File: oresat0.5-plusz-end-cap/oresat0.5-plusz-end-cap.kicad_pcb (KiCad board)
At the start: 2 copper layers, 105.6 x 105.6 mm, 43 parts, among them J2 U.FL-R-SMA, U1 LTC4305, U2 MMC5983MA, U3 MMC5983MA

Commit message: Oresat 0.5 +z end cap v1.3 ready for ordering!
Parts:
- removed @HOLE0, @HOLE1, @HOLE2, @HOLE3, @HOLE6, @HOLE7: MountingHole_2.1mm, MountingHole:MountingHole_2.1mm
- added @HOLE4: MountingHole_2.1mm, MountingHole:MountingHole_2.1mm, F.Cu at (198.0, 132.5)
- added @HOLE4: MountingHole_2.1mm, MountingHole:MountingHole_2.1mm, F.Cu at (176.0, 55.5)
- added @HOLE4: MountingHole_2.1mm, MountingHole:MountingHole_2.1mm, F.Cu at (198.0, 77.5)
- added @HOLE4: MountingHole_2.1mm, MountingHole:MountingHole_2.1mm, F.Cu at (121.0, 154.5)
- added @HOLE4: MountingHole_2.1mm, MountingHole:MountingHole_2.1mm, F.Cu at (176.0, 154.5)
- added @HOLE4: MountingHole_2.1mm, MountingHole:MountingHole_2.1mm, F.Cu at (121.0, 55.5)
- added LOGO1: , oresat-graphics:PSAS_LOGO_10X10, F.Cu at (183.5, 148.2)
- added REF**: logo-small, oresat-graphics:logo-small, F.Cu at (192.8, 139.0)
- C1, C10, C2, C3, C7: value ~ -> 100n
- C12, C13, C4: value ~ -> 10u
- D2, J1, R1, R10, R3, R4, R5, R6, R7, R8, R9: value ~ -> 4.7k
- R2: value ~ -> 2.7k
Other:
- board text added: "2024/03/20"
- board text removed: "2024/03/04"

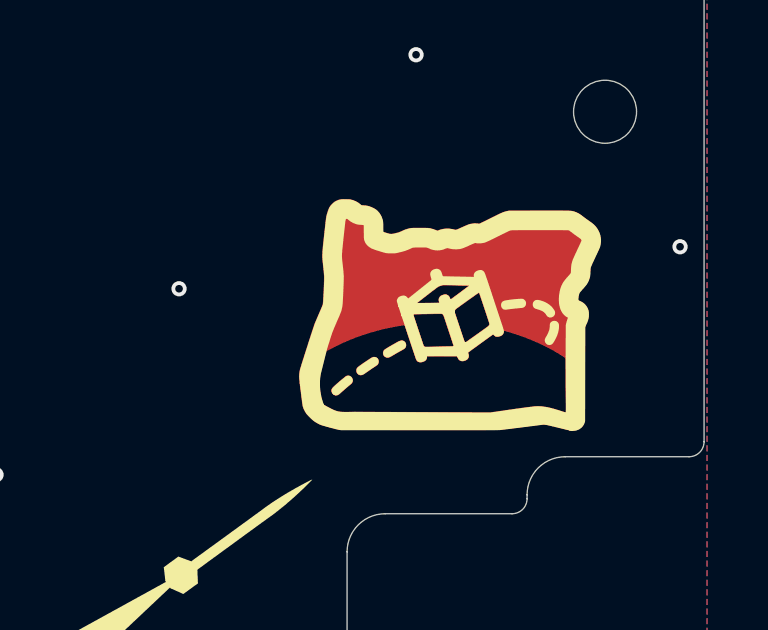
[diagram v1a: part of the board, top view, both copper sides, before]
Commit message: OreSat 0.5 Endcaps (+Z v1.3 and -Z v1.2) ready for ordering, reviewed -Z endcap, made small library and neatness changes to +Z endcap
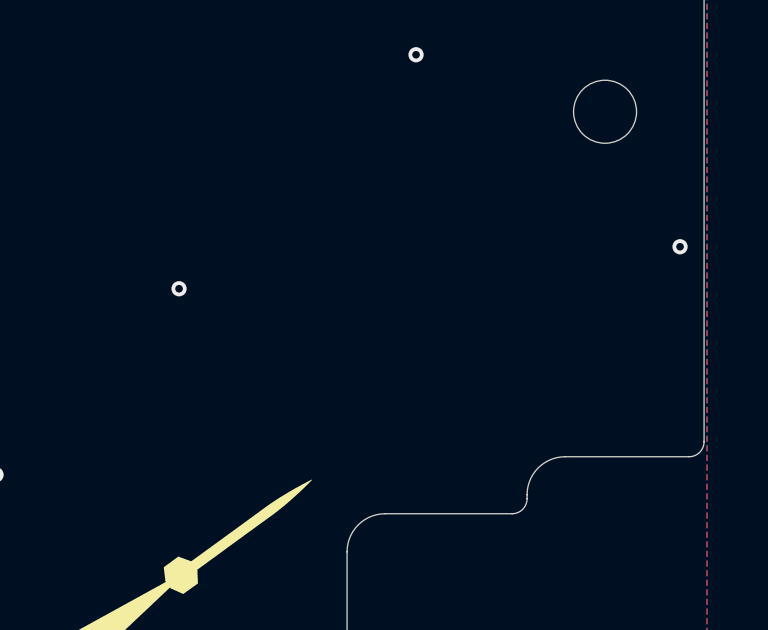
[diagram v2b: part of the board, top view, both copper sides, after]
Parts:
- removed REF**: logo-small, oresat-graphics:logo-small
- U1: footprint oresat0.5-plusz-end-cap:16-SSOP -> oresat-ics:16-SSOP

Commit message: Fixed issues 5 and 6 -- weird 4.7k values everywhere, missing libraries, and used no-place to indicate actual no place components.
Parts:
- D2: value 4.7k -> GRN
- J1: value 4.7k -> M55-7011242R
- R11, R12: value NP -> 2.7k
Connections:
- net 3.3V renamed +3.3V
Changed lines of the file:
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@@
 	)
 	(net 0 "")
-	(net 1 "3.3V")
+	(net 1 "+3.3V")
 	(net 2 "GND")
 	(net 3 "Net-(ANT1-A)")
@@
 		(sheetname "Root")
 		(sheetfile "oresat0.5-plusz-end-cap.kicad_sch")
-		(attr smd)
+		(attr smd dnp)
 		(fp_line
 			(start -0.885 -1.4)
@@
 			(layers "*.Cu" "*.Mask")
 			(remove_unused_layers no)
-			(net 1 "3.3V")
+			(net 1 "+3.3V")
 			(pinfunction "1")
 			(pintype "passive")
@@
 		(sheetname "Root")
 		(sheetfile "oresat0.5-plusz-end-cap.kicad_sch")
-		(attr smd)
+		(attr smd dnp)
 		(fp_rect
 			(start -1.4 3.1)
@@
 			)
 		)
-		(property "Value" "4.7k"
+		(property "Value" "GRN"
 			(at 0 0.635 0)
 			(layer "F.Fab")
@@
 			)
 		)
-		(property "Value" "4.7k"
+		(property "Value" "M55-7011242R"
 			(at 0 0 90)
 			(layer "B.Fab")
@@
 			(size 0.8 1.1)
 			(layers "B.Cu" "B.Paste" "B.Mask")
-			(net 1 "3.3V")
+			(net 1 "+3.3V")
 			(pinfunction "5")
 			(pintype "passive")
@@
 			(size 0.8 1.1)
 			(layers "B.Cu" "B.Paste" "B.Mask")
-			(net 1 "3.3V")
+			(net 1 "+3.3V")
 			(pinfunction "6")
 			(pintype "passive")
@@
 			(layers "B.Cu" "B.Paste" "B.Mask")
 			(roundrect_rratio 0.25)
-			(net 1 "3.3V")
+			(net 1 "+3.3V")
 			(pinfunction "2")
 			(pintype "passive")
@@
 			(layers "B.Cu" "B.Paste" "B.Mask")
 			(roundrect_rratio 0.25)
-			(net 1 "3.3V")
+			(net 1 "+3.3V")
 			(pinfunction "1")
 			(pintype "passive")
@@
 			(layers "B.Cu" "B.Paste" "B.Mask")
 			(roundrect_rratio 0.25)
-			(net 1 "3.3V")
+			(net 1 "+3.3V")
 			(pinfunction "1")
 			(pintype "passive")
@@
 			(layers "B.Cu" "B.Paste" "B.Mask")
 			(roundrect_rratio 0.25)
-			(net 1 "3.3V")
+			(net 1 "+3.3V")
 			(pinfunction "2")
 			(pintype "passive")
@@
 			(layers "B.Cu" "B.Paste" "B.Mask")
 			(roundrect_rratio 0.25)
-			(net 1 "3.3V")
+			(net 1 "+3.3V")
 			(pinfunction "2")
 			(pintype "passive")
@@
 			)
 		)
-		(property "Value" "NP"
+		(property "Value" "2.7k"
 			(at -1.2 -1.6 90)
 			(layer "B.Fab")
@@
 		(sheetname "Root")
 		(sheetfile "oresat0.5-plusz-end-cap.kicad_sch")
+		(attr dnp)
 		(fp_line
 			(start 1.495 -0.745)
@@
 			(layers "B.Cu" "B.Paste" "B.Mask")
 			(roundrect_rratio 0.25)
-			(net 1 "3.3V")
+			(net 1 "+3.3V")
 			(pinfunction "2")
 			(pintype "passive")
@@
 			(size 0.3 0.45)
 			(layers "B.Cu" "B.Paste" "B.Mask")
-			(net 1 "3.3V")
+			(net 1 "+3.3V")
 			(pinfunction "VDD")
 			(pintype "power_in")
@@
 			(size 0.3 0.45)
 			(layers "B.Cu" "B.Paste" "B.Mask")
-			(net 1 "3.3V")
+			(net 1 "+3.3V")
 			(pinfunction "SPI_CS")
 			(pintype "input")
@@
 			(size 0.3 0.45)
 			(layers "B.Cu" "B.Paste" "B.Mask")
-			(net 1 "3.3V")
+			(net 1 "+3.3V")
 			(pinfunction "VDDIO")
 			(pintype "power_in")
@@
 			(size 0.3 0.45)
 			(layers "B.Cu" "B.Paste" "B.Mask")
-			(net 1 "3.3V")
+			(net 1 "+3.3V")
 			(pinfunction "VDD")
 			(pintype "power_in")
@@
 			(size 0.3 0.45)
 			(layers "B.Cu" "B.Paste" "B.Mask")
-			(net 1 "3.3V")
+			(net 1 "+3.3V")
 			(pinfunction "SPI_CS")
 			(pintype "input")
@@
 			(size 0.3 0.45)
 			(layers "B.Cu" "B.Paste" "B.Mask")
-			(net 1 "3.3V")
+			(net 1 "+3.3V")
 			(pinfunction "VDDIO")
 			(pintype "power_in")
@@
 			(layers "B.Cu" "B.Paste" "B.Mask")
 			(roundrect_rratio 0.25)
-			(net 1 "3.3V")
+			(net 1 "+3.3V")
 			(pinfunction "2")
 			(pintype "passive")
@@
 			(layers "B.Cu" "B.Paste" "B.Mask")
 			(roundrect_rratio 0.25)
-			(net 1 "3.3V")
+			(net 1 "+3.3V")
 			(pinfunction "1")
 			(pintype "passive")
@@
 			(layers "B.Cu" "B.Paste" "B.Mask")
 			(roundrect_rratio 0.25)
-			(net 1 "3.3V")
+			(net 1 "+3.3V")
 			(pinfunction "2")
 			(pintype "passive")
@@
 			(layers "B.Cu" "B.Paste" "B.Mask")
 			(roundrect_rratio 0.25)
-			(net 1 "3.3V")
+			(net 1 "+3.3V")
 			(pinfunction "1")
 			(pintype "passive")
@@
 			(layers "B.Cu" "B.Paste" "B.Mask")
 			(roundrect_rratio 0.25)
-			(net 1 "3.3V")
+			(net 1 "+3.3V")
 			(pinfunction "1")
 			(pintype "passive")
@@
 			(layers "B.Cu" "B.Paste" "B.Mask")
 			(roundrect_rratio 0.25)
-			(net 1 "3.3V")
+			(net 1 "+3.3V")
 			(pinfunction "2")
 			(pintype "passive")
@@
 			(size 1.143 0.4191)
 			(layers "B.Cu" "B.Paste" "B.Mask")
-			(net 1 "3.3V")
+			(net 1 "+3.3V")
 			(pinfunction "VCC")
 			(pintype "power_in")
@@
 			(layers "B.Cu" "B.Paste" "B.Mask")
 			(roundrect_rratio 0.25)
-			(net 1 "3.3V")
+			(net 1 "+3.3V")
 			(pinfunction "2")
 			(pintype "passive")
@@
 			(layers "B.Cu" "B.Paste" "B.Mask")
 			(roundrect_rratio 0.25)
-			(net 1 "3.3V")
+			(net 1 "+3.3V")
 			(pinfunction "1")
 			(pintype "passive")
@@
 			)
 		)
-		(property "Value" "NP"
+		(property "Value" "2.7k"
 			(at -1.2 -1.6 0)
 			(layer "B.Fab")
@@
 		(sheetname "Root")
 		(sheetfile "oresat0.5-plusz-end-cap.kicad_sch")
+		(attr dnp)
 		(fp_line
 			(start 1.495 0.745)
